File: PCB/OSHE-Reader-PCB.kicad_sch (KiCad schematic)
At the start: 0 parts

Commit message: New PCB Files with the fotprints I could find
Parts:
- added U1: ESP32-S3-WROOM-1-N8R8, ESP32-S3-WROOM-1-N8R8:XCVR_ESP32S3WROOM1N8R8, symbol ESP32-S3-WROOM-1-N8R8:ESP32-S3-WROOM-1-N8R8

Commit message: Actually working now I think
Got new footprints working mainly for the esp
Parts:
- U1: footprint ESP32-S3-WROOM-1-N8R8:XCVR_ESP32S3WROOM1N8R8 -> ESP32_S3_WROOM_1_N8R8:XCVR_ESP32S3WROOM1N8R8; AVAILABILITY In Stock -> (none); PRICE None -> (none); PURCHASE-URL https://pricing.snapeda.com/search/part/ESP32S3WROOM1N8R8/?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 -> (none)
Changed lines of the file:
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@@
 	(symbol
 		(lib_id "ESP32-S3-WROOM-1-N8R8:ESP32-S3-WROOM-1-N8R8")
-		(at 86.36 59.69 0)
+		(at 59.69 62.23 0)
 		(unit 1)
 		(body_style 1)
@@
 		(fields_autoplaced yes)
 		(property "Reference" "U1"
-			(at 86.36 21.59 0)
+			(at 59.69 21.59 0)
 			(show_name no)
 			(do_not_autoplace no)
@@
 		)
 		(property "Value" "ESP32-S3-WROOM-1-N8R8"
-			(at 86.36 24.13 0)
-			(show_name no)
-			(do_not_autoplace no)
-			(effects
-				(font
-					(size 1.27 1.27)
-				)
-			)
-		)
-		(property "Footprint" "ESP32-S3-WROOM-1-N8R8:XCVR_ESP32S3WROOM1N8R8"
-			(at 86.36 59.69 0)
-			(hide yes)
-			(show_name no)
-			(do_not_autoplace no)
-			(effects
-				(font
-					(size 1.27 1.27)
-				)
-				(justify bottom)
+			(at 59.69 24.13 0)
+			(show_name no)
+			(do_not_autoplace no)
+			(effects
+				(font
+					(size 1.27 1.27)
+				)
+			)
+		)
+		(property "Footprint" "ESP32_S3_WROOM_1_N8R8:XCVR_ESP32S3WROOM1N8R8"
+			(at 59.69 26.67 0)
+			(show_name no)
+			(do_not_autoplace no)
+			(effects
+				(font
+					(size 1.27 1.27)
+				)
 			)
 		)
 		(property "Datasheet" ""
-			(at 86.36 59.69 0)
+			(at 59.69 62.23 0)
 			(hide yes)
 			(show_name no)
@@
 		)
 		(property "Description" "Bluetooth, WiFi 802.11b/g/n, Bluetooth v5.0 Transceiver Module 2.4GHz PCB Trace Surface Mount"
-			(at 86.36 59.69 0)
+			(at 59.69 62.23 0)
 			(hide yes)
 			(show_name no)
@@
 		)
 		(property "MF" "Espressif Systems"
-			(at 86.36 59.69 0)
+			(at 59.69 62.23 0)
 			(hide yes)
 			(show_name no)
@@
 		)
 		(property "PACKAGE" "SMD-41 Espressif Systems"
-			(at 86.36 59.69 0)
-			(hide yes)
-			(show_name no)
-			(do_not_autoplace no)
-			(effects
-				(font
-					(size 1.27 1.27)
-				)
-				(justify bottom)
-			)
-		)
-		(property "PRICE" "None"
-			(at 86.36 59.69 0)
+			(at 59.69 62.23 0)
+			(hide yes)
+			(show_name no)
+			(do_not_autoplace no)
+			(effects
+				(font
+					(size 1.27 1.27)
+				)
+				(justify bottom)
+			)
+		)
+		(property "PRICE" ""
+			(at 59.69 62.23 0)
 			(hide yes)
 			(show_name no)
@@
 		)
 		(property "MP" "ESP32S3WROOM1N8R8"
-			(at 86.36 59.69 0)
-			(hide yes)
-			(show_name no)
-			(do_not_autoplace no)
-			(effects
-				(font
-					(size 1.27 1.27)
-				)
-				(justify bottom)
-			)
-		)
-		(property "AVAILABILITY" "In Stock"
-			(at 86.36 59.69 0)
-			(hide yes)
-			(show_name no)
-			(do_not_autoplace no)
-			(effects
-				(font
-					(size 1.27 1.27)
-				)
-				(justify bottom)
-			)
-		)
-		(property "PURCHASE-URL" "https://pricing.snapeda.com/search/part/ESP32S3WROOM1N8R8/?ref=eda"
-			(at 86.36 59.69 0)
-			(hide yes)
-			(show_name no)
-			(do_not_autoplace no)
-			(effects
-				(font
-					(size 1.27 1.27)
-				)
-				(justify bottom)
-			)
+			(at 59.69 62.23 0)
+			(hide yes)
+			(show_name no)
+			(do_not_autoplace no)
+			(effects
+				(font
+					(size 1.27 1.27)
+				)
+				(justify bottom)
+			)
+		)
+		(property "AVAILABILITY" ""
+			(at 59.69 62.23 0)
+			(hide yes)
+			(show_name no)
+			(do_not_autoplace no)
+			(effects
+				(font
+					(size 1.27 1.27)
+				)
+				(justify bottom)
+			)
+		)
+		(property "PURCHASE-URL" ""
+			(at 59.69 62.23 0)
+			(hide yes)
+			(show_name no)
+			(do_not_autoplace no)
+			(effects
+				(font
+					(size 1.27 1.27)
+				)
+				(justify bottom)
+			)
+		)
+		(pin "6"
+		)
+		(pin "8"
+		)
+		(pin "7"
+		)
+		(pin "5"
+		)
+		(pin "9"
+		)
+		(pin "14"
+		)
+		(pin "10"
+		)
+		(pin "12"
+		)
+		(pin "11"
+		)
+		(pin "13"
+		)
+		(pin "19"
+		)
+		(pin "16"
+		)
+		(pin "17"
+		)
+		(pin "18"
+		)
+		(pin "15"
+		)
+		(pin "3"
 		)
 		(pin "2"
 		)
-		(pin "5"
-		)
-		(pin "9"
-		)
-		(pin "11"
-		)
-		(pin "8"
-		)
-		(pin "19"
-		)
-		(pin "7"
-		)
-		(pin "14"
-		)
-		(pin "13"
-		)
-		(pin "16"
-		)
-		(pin "6"
-		)
-		(pin "3"
-		)
 		(pin "1"
 		)
-		(pin "18"
-		)
-		(pin "12"
-		)
-		(pin "17"
-		)
-		(pin "15"
-		)
 		(pin "4"
 		)
-		(pin "10"
+		(pin "41_6"
+		)
+		(pin "41_3"
+		)
+		(pin "41_4"
+		)
+		(pin "24"
+		)
+		(pin "41_7"
+		)
+		(pin "28"
 		)
 		(pin "23"
 		)
+		(pin "27"
+		)
+		(pin "41_5"
+		)
+		(pin "39"
+		)
+		(pin "41_8"
+		)
+		(pin "26"
+		)
+		(pin "35"
+		)
+		(pin "22"
+		)
+		(pin "34"
+		)
+		(pin "31"
+		)
+		(pin "25"
+		)
+		(pin "37"
+		)
+		(pin "40"
+		)
+		(pin "30"
+		)
+		(pin "21"
+		)
+		(pin "33"
+		)
+		(pin "38"
+		)
+		(pin "36"
+		)
+		(pin "20"
+		)
+		(pin "29"
+		)
+		(pin "41_2"
+		)
+		(pin "41_1"
+		)
 		(pin "32"
 		)
-		(pin "41_5"
-		)
-		(pin "41_1"
-		)
-		(pin "41_2"
-		)
-		(pin "41_6"
-		)
-		(pin "35"
-		)
-		(pin "25"
-		)
-		(pin "41_8"
-		)
-		(pin "41_7"
-		)
-		(pin "37"
-		)
-		(pin "34"
-		)
-		(pin "27"
-		)
-		(pin "30"
-		)
-		(pin "33"
-		)
-		(pin "39"
-		)
-		(pin "22"
-		)
-		(pin "40"
-		)
-		(pin "41_3"
-		)
-		(pin "21"
-		)
-		(pin "24"
-		)
-		(pin "28"
-		)
-		(pin "31"
-		)
-		(pin "41_4"
-		)
-		(pin "36"
-		)
-		(pin "20"
-		)
-		(pin "38"
-		)
-		(pin "26"
-		)
-		(pin "29"
-		)
 		(pin "41_9"

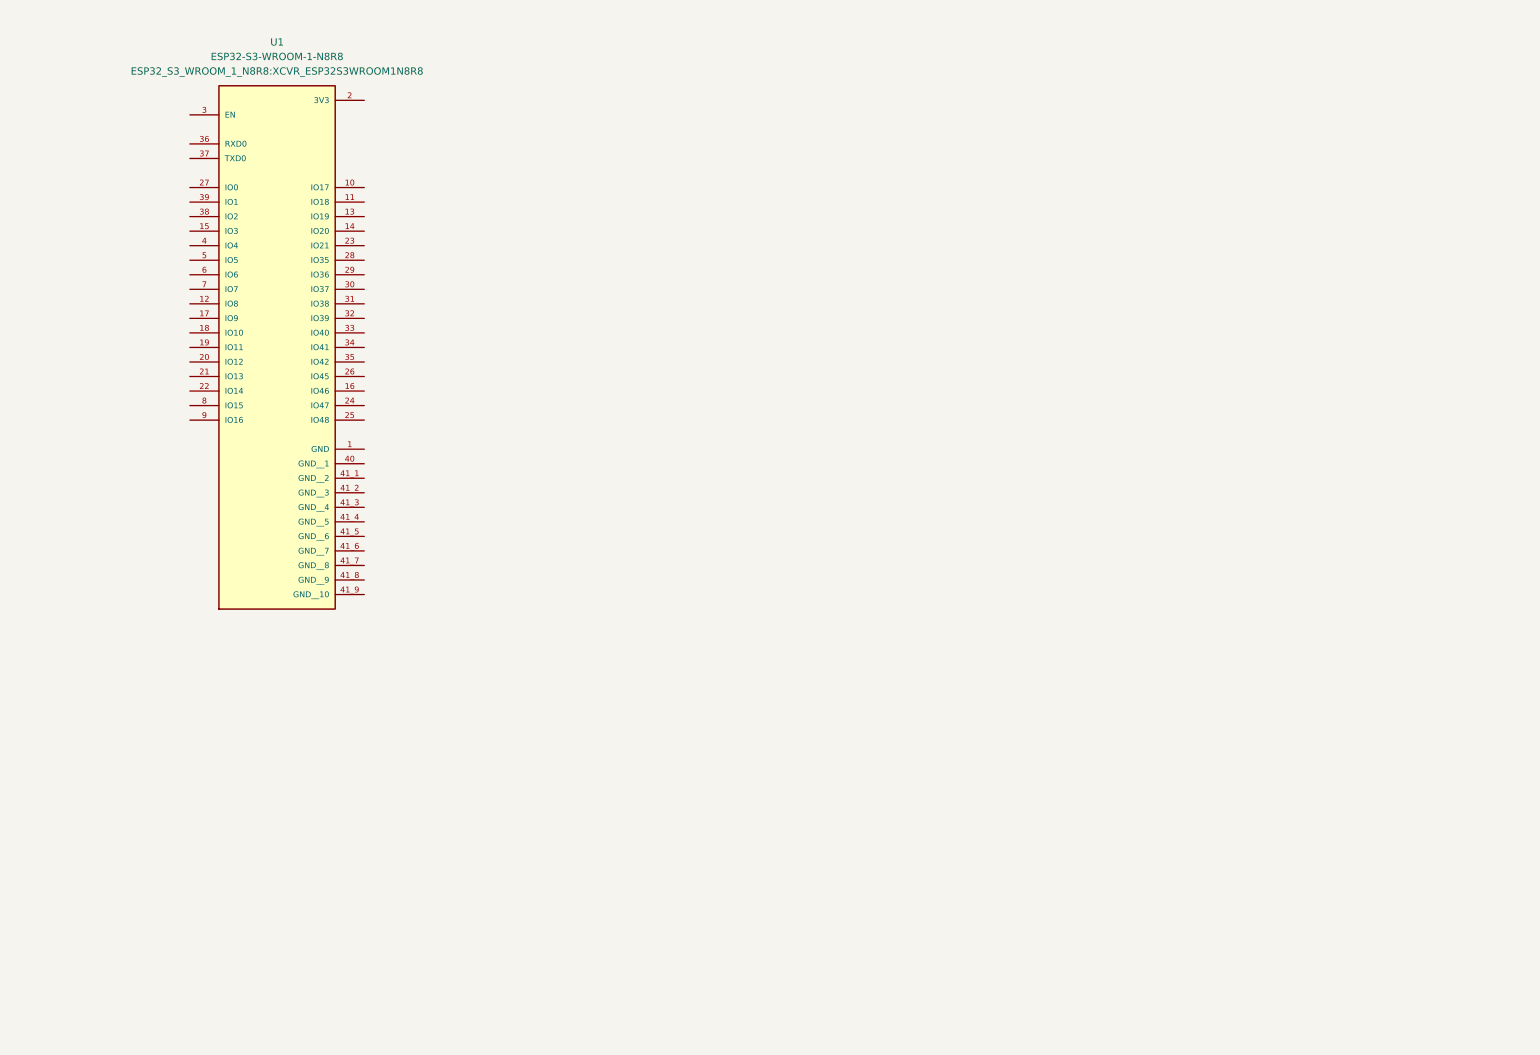
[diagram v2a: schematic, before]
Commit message: Added footprints + populated schematic
TODO: wiring
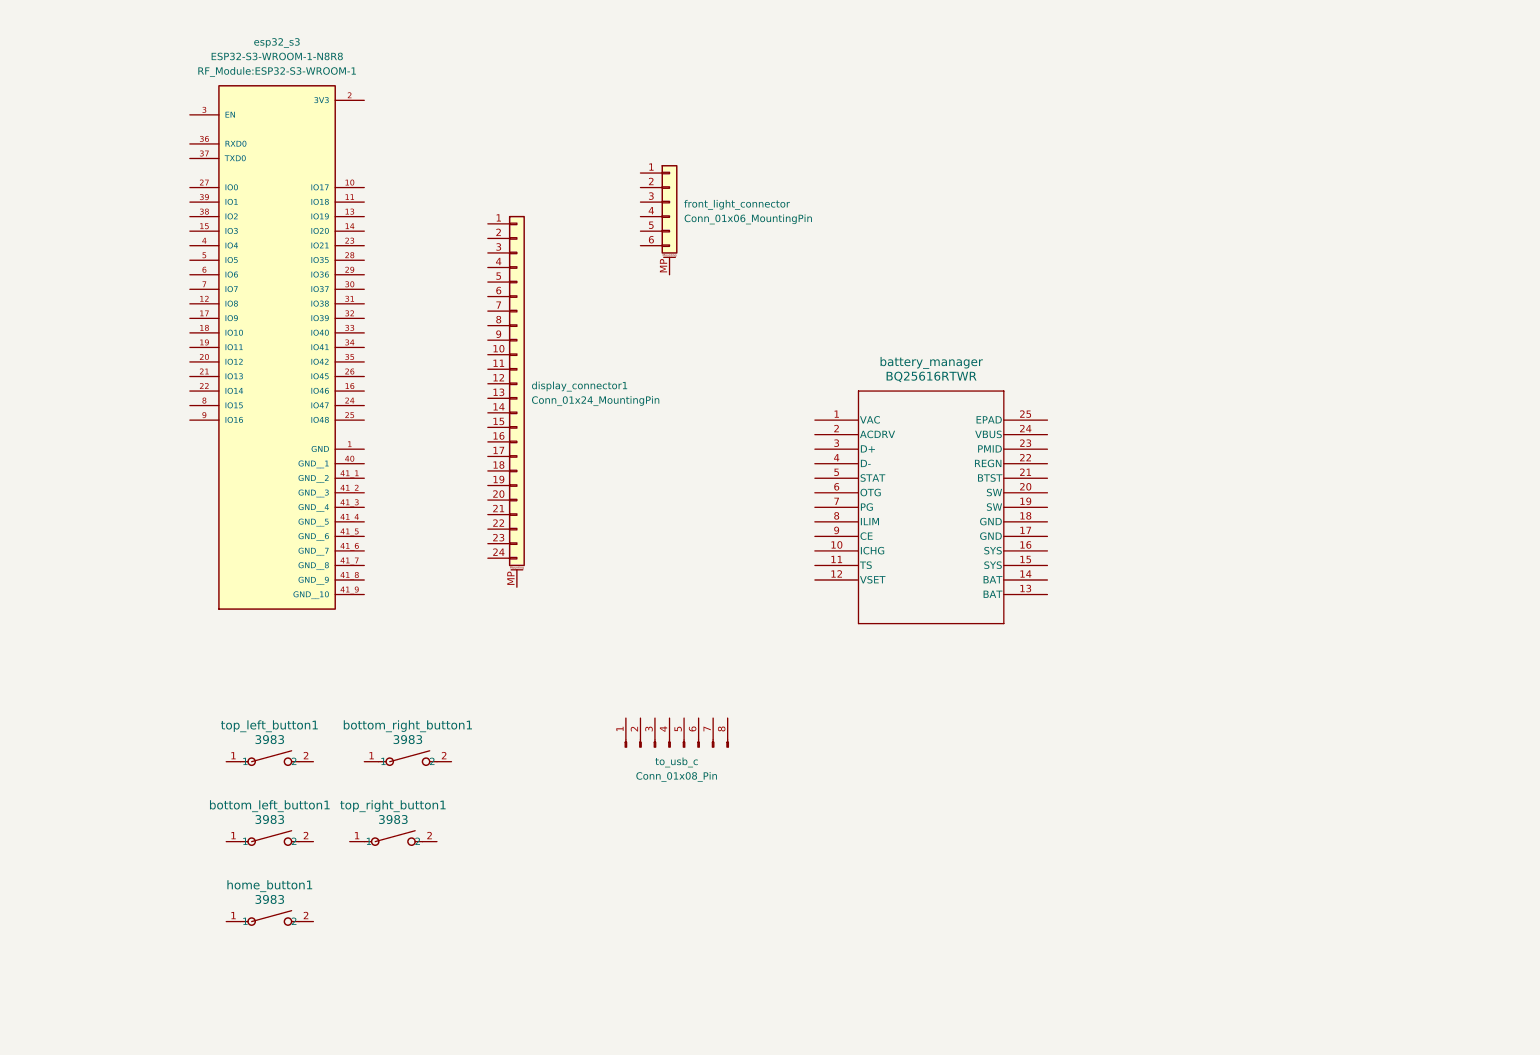
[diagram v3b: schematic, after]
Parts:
- added battery_manager: BQ25616RTWR, BQ25616RTWR:QFN24_RTW_TEX, symbol BQ25616RTWR:BQ25616RTWR
- added bottom_left_button1, bottom_right_button1, home_button1, top_left_button1, top_right_button1: 3983, Adafruit 3983:SW_3983_ADA, symbol Adafruit 3983:3983
- added display_connector1: Conn_01x24_MountingPin, Connector_FFC-FPC:Hirose_FH12-24S-0.5SH_1x24-1MP_P0.50mm_Horizontal, symbol Connector_Generic_MountingPin:Conn_01x24_MountingPin
- added front_light_connector: Conn_01x06_MountingPin, Connector_FFC-FPC:Hirose_FH12-6S-0.5SH_1x06-1MP_P0.50mm_Horizontal, symbol Connector_Generic_MountingPin:Conn_01x06_MountingPin
- added to_usb_c: Conn_01x08_Pin, Connector_PinHeader_2.54mm:PinHeader_1x08_P2.54mm_Vertical, symbol Connector:Conn_01x08_Pin
- esp32_s3: renamed from U1; footprint ESP32_S3_WROOM_1_N8R8:XCVR_ESP32S3WROOM1N8R8 -> RF_Module:ESP32-S3-WROOM-1

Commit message: Added JST
forgot battery connector :(
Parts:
- added to_battery: Conn_01x02_Pin, Connector_JST:JST_PH_S2B-PH-K_1x02_P2.00mm_Horizontal, symbol Connector:Conn_01x02_Pin
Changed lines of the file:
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@@
+	)
+	(symbol
+		(lib_id "Connector:Conn_01x02_Pin")
+		(at 163.83 139.7 0)
+		(unit 1)
+		(body_style 1)
+		(exclude_from_sim no)
+		(in_bom yes)
+		(on_board yes)
+		(in_pos_files yes)
+		(dnp no)
+		(fields_autoplaced yes)
+		(property "Reference" "to_battery"
+			(at 164.465 134.62 0)
+			(show_name no)
+			(do_not_autoplace no)
+			(effects
+				(font
+					(size 1.27 1.27)
+				)
+			)
+		)
+		(property "Value" "Conn_01x02_Pin"
+			(at 164.465 137.16 0)
+			(show_name no)
+			(do_not_autoplace no)
+			(effects
+				(font
+					(size 1.27 1.27)
+				)
+			)
+		)
+		(property "Footprint" "Connector_JST:JST_PH_S2B-PH-K_1x02_P2.00mm_Horizontal"
+			(at 163.83 139.7 0)
+			(hide yes)
+			(show_name no)
+			(do_not_autoplace no)
+			(effects
+				(font
+					(size 1.27 1.27)
+				)
+			)
+		)
+		(property "Datasheet" ""
+			(at 163.83 139.7 0)
+			(hide yes)
+			(show_name no)
+			(do_not_autoplace no)
+			(effects
+				(font
+					(size 1.27 1.27)
+				)
+			)
+		)
+		(property "Description" "Generic connector, single row, 01x02, script generated"
+			(at 163.83 139.7 0)
+			(hide yes)
+			(show_name no)
+			(do_not_autoplace no)
+			(effects
+				(font
+					(size 1.27 1.27)
+				)
+			)
+		)
+		(pin "1"
+		)
+		(pin "2"
+		)
+		(instances
+			(project "OSHE-Reader-PCB"
+				(path "/f297096e-4a95-4c17-b91a-21f33415233d"
+					(reference "to_battery")
+					(unit 1)
+				)
+			)
+		)
 	)
 	(symbol

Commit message: battery connector
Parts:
- removed to_battery: Conn_01x02_Pin, Connector_JST:JST_PH_S2B-PH-K_1x02_P2.00mm_Horizontal, symbol Connector:Conn_01x02_Pin
- added to_battery: Conn_01x02_MountingPin, Connector_JST:JST_PH_S2B-PH-SM4-TB_1x02-1MP_P2.00mm_Horizontal, symbol Connector_Generic_MountingPin:Conn_01x02_MountingPin
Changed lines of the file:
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@@
 	)
 	(symbol
-		(lib_id "Connector:Conn_01x02_Pin")
-		(at 163.83 139.7 0)
+		(lib_id "Connector_Generic_MountingPin:Conn_01x02_MountingPin")
+		(at 168.91 135.89 0)
 		(unit 1)
 		(body_style 1)
@@
 		(fields_autoplaced yes)
 		(property "Reference" "to_battery"
-			(at 164.465 134.62 0)
+			(at 171.45 136.2455 0)
 			(show_name no)
 			(do_not_autoplace no)
@@
 					(size 1.27 1.27)
 				)
+				(justify left)
 			)
 		)
-		(property "Value" "Conn_01x02_Pin"
-			(at 164.465 137.16 0)
+		(property "Value" "Conn_01x02_MountingPin"
+			(at 171.45 138.7855 0)
 			(show_name no)
 			(do_not_autoplace no)
@@
 					(size 1.27 1.27)
 				)
+				(justify left)
 			)
 		)
-		(property "Footprint" "Connector_JST:JST_PH_S2B-PH-K_1x02_P2.00mm_Horizontal"
-			(at 163.83 139.7 0)
+		(property "Footprint" "Connector_JST:JST_PH_S2B-PH-SM4-TB_1x02-1MP_P2.00mm_Horizontal"
+			(at 168.91 135.89 0)
 			(hide yes)
 			(show_name no)
@@
 		)
 		(property "Datasheet" ""
-			(at 163.83 139.7 0)
+			(at 168.91 135.89 0)
 			(hide yes)
 			(show_name no)
@@
 			)
 		)
-		(property "Description" "Generic connector, single row, 01x02, script generated"
-			(at 163.83 139.7 0)
+		(property "Description" "Generic connectable mounting pin connector, single row, 01x02, script generated (kicad-library-utils/schlib/autogen/connector/)"
+			(at 168.91 135.89 0)
 			(hide yes)
 			(show_name no)
@@
 			)
 		)
+		(pin "2"
+		)
 		(pin "1"
 		)
-		(pin "2"
+		(pin "MP"
 		)
 		(instances
